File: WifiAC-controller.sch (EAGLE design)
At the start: 10 parts

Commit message: fixed schematic and generated layout
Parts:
- DRV_PINS, PWR_IN: device SparkFun-Connectors:M02PTH3 -> SparkFun-Connectors:M02LOCK_LONGPADS
- R2: device SparkFun-Resistors:RESISTOR1206 -> SparkFun-Resistors:RESISTORPTH-1/4W
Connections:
- net GPIO12: now also QBS_B.C; no longer QBS_C.B
- net GPIO13: now also QBS_C.C; no longer QBS_D.B
- net GPIO14: now also QBS_D.C; no longer QBS_B.B
- net GPIO16: now also QBS_A.C; no longer QBS_A.B
- net P59: now also QBS_C.B, QBS_D.B; no longer QBS_C.C, QBS_D.C
- net P7: now also QBS_A.B, QBS_B.B; no longer QBS_A.C, QBS_B.C

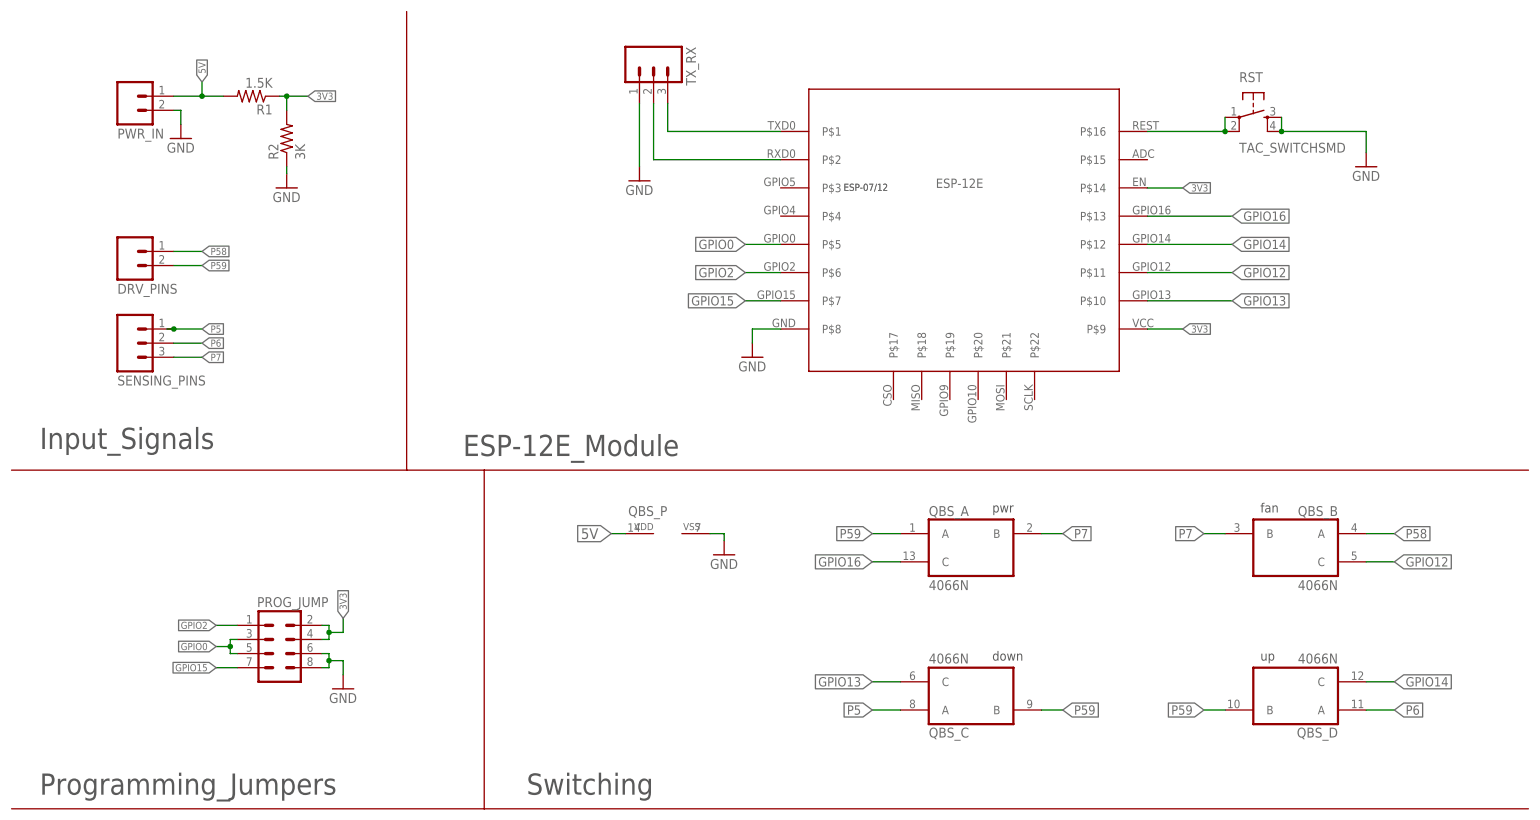
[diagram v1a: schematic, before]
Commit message: updated schematic to add input connections for the esp module
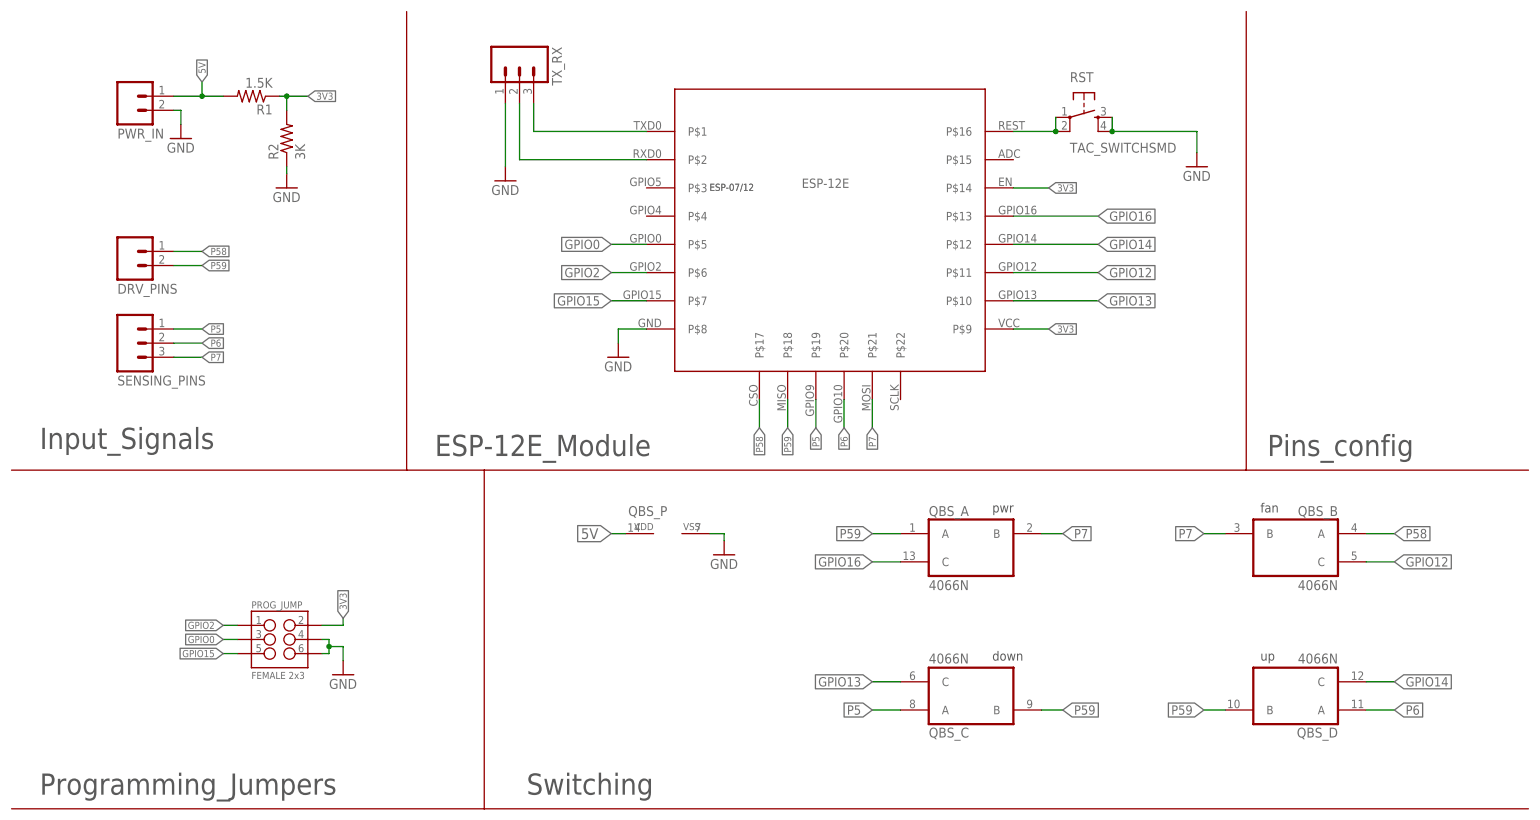
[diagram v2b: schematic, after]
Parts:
- PROG_JUMP: value (none) -> FEMALE 2x3; device SparkFun-Connectors:M04X2 -> SparkFun-Connectors:M03X2FEMALE
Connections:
- net 3V3: no longer PROG_JUMP.4
- net GND: now also PROG_JUMP.4; no longer PROG_JUMP.8
- net GPIO0: no longer PROG_JUMP.5
- net GPIO15: now also PROG_JUMP.5; no longer PROG_JUMP.7
- net P5: now also ESP-12E.P$19
- net P58: now also ESP-12E.P$17
- net P59: now also ESP-12E.P$18
- net P6: now also ESP-12E.P$20
- net P7: now also ESP-12E.P$21
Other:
- note added: "INPUT PINS"
- note added: "OUTPUT PINS"
- note added: "Pins_config"
- note added: "down -> GPIO13"
- note added: "fan -> GPIO12"
- note added: "p5 -> GPIO9"
- note added: "p58 -> GPIO11"
- note added: "p59 -> GPIO7"
- note added: "p6 -> GPIO10"
- note added: "p7 -> GPIO8"
- note added: "pwr -> GPIO16"
- note added: "up -> GPIO14"
- moved on the sheet: RST, TX_RX

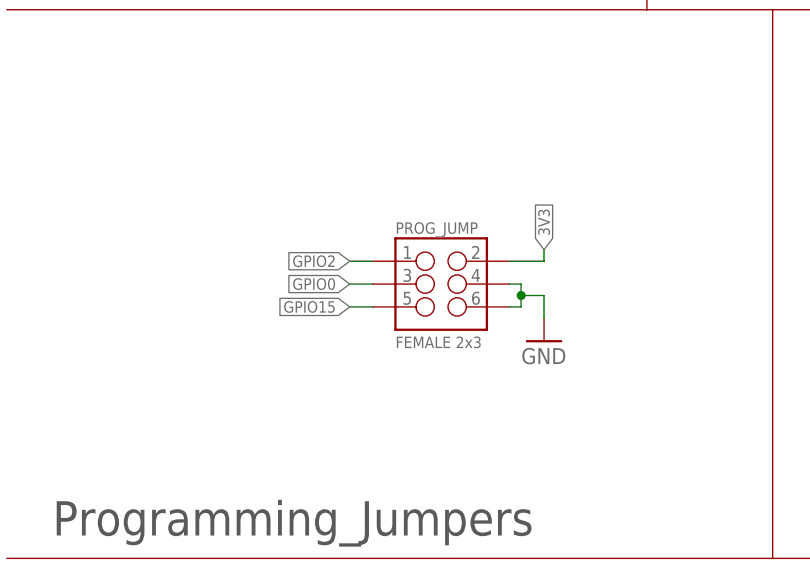
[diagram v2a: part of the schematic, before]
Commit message: updated layout
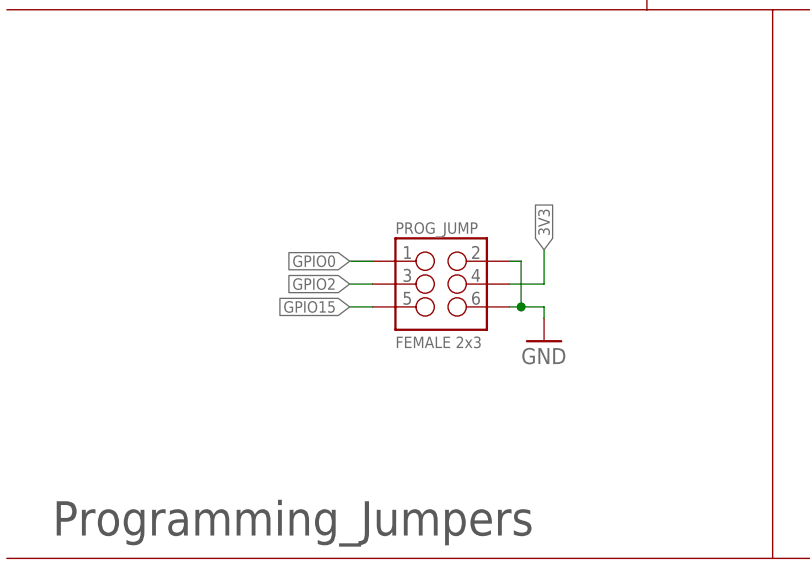
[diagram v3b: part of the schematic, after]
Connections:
- net 3V3: now also PROG_JUMP.4; no longer PROG_JUMP.2
- net GND: now also PROG_JUMP.2; no longer PROG_JUMP.4
- net GPIO0: now also PROG_JUMP.1; no longer PROG_JUMP.3
- net GPIO2: now also PROG_JUMP.3; no longer PROG_JUMP.1
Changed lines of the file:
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@@
 </segment>
 <segment>
-<pinref part="PROG_JUMP" gate="G$1" pin="2"/>
-<wire x1="55.88" y1="68.58" x2="59.69" y2="68.58" width="0.1524" layer="91"/>
-<wire x1="59.69" y1="68.58" x2="59.69" y2="69.85" width="0.1524" layer="91"/>
 <label x="59.69" y="69.85" size="1.27" layer="95" font="vector" rot="R90" xref="yes"/>
+<wire x1="59.69" y1="69.85" x2="59.69" y2="66.04" width="0.1524" layer="91"/>
+<pinref part="PROG_JUMP" gate="G$1" pin="4"/>
+<wire x1="59.69" y1="66.04" x2="55.88" y2="66.04" width="0.1524" layer="91"/>
 </segment>
 </net>
@@
 </segment>
 <segment>
-<wire x1="57.15" y1="64.77" x2="59.69" y2="64.77" width="0.1524" layer="91"/>
-<wire x1="59.69" y1="64.77" x2="59.69" y2="62.23" width="0.1524" layer="91"/>
+<wire x1="55.88" y1="63.5" x2="57.15" y2="63.5" width="0.1524" layer="91"/>
+<wire x1="57.15" y1="63.5" x2="59.69" y2="63.5" width="0.1524" layer="91"/>
+<wire x1="59.69" y1="63.5" x2="59.69" y2="62.23" width="0.1524" layer="91"/>
 <pinref part="GND6" gate="1" pin="GND"/>
-<pinref part="PROG_JUMP" gate="G$1" pin="4"/>
-<wire x1="55.88" y1="66.04" x2="57.15" y2="66.04" width="0.1524" layer="91"/>
-<wire x1="57.15" y1="66.04" x2="57.15" y2="64.77" width="0.1524" layer="91"/>
 <pinref part="PROG_JUMP" gate="G$1" pin="6"/>
-<wire x1="55.88" y1="63.5" x2="57.15" y2="63.5" width="0.1524" layer="91"/>
-<wire x1="57.15" y1="63.5" x2="57.15" y2="64.77" width="0.1524" layer="91"/>
-<junction x="57.15" y="64.77"/>
+<pinref part="PROG_JUMP" gate="G$1" pin="2"/>
+<wire x1="55.88" y1="68.58" x2="57.15" y2="68.58" width="0.1524" layer="91"/>
+<wire x1="57.15" y1="68.58" x2="57.15" y2="63.5" width="0.1524" layer="91"/>
+<junction x="57.15" y="63.5"/>
 </segment>
 <segment>
@@
 </segment>
 <segment>
+<pinref part="PROG_JUMP" gate="G$1" pin="1"/>
+<wire x1="40.64" y1="68.58" x2="38.1" y2="68.58" width="0.1524" layer="91"/>
+<label x="38.1" y="68.58" size="1.27" layer="95" rot="R180" xref="yes"/>
+</segment>
+</net>
+<net name="GPIO2" class="0">
+<segment>
+<pinref part="ESP-12E" gate="G$1" pin="P$6"/>
+<wire x1="114.3" y1="132.08" x2="107.95" y2="132.08" width="0.1524" layer="91"/>
+<label x="107.95" y="132.08" size="1.6764" layer="95" rot="R180" xref="yes"/>
+</segment>
+<segment>
 <pinref part="PROG_JUMP" gate="G$1" pin="3"/>
 <wire x1="40.64" y1="66.04" x2="38.1" y2="66.04" width="0.1524" layer="91"/>
@@
 </segment>
 </net>
-<net name="GPIO2" class="0">
-<segment>
-<pinref part="ESP-12E" gate="G$1" pin="P$6"/>
-<wire x1="114.3" y1="132.08" x2="107.95" y2="132.08" width="0.1524" layer="91"/>
-<label x="107.95" y="132.08" size="1.6764" layer="95" rot="R180" xref="yes"/>
-</segment>
-<segment>
-<pinref part="PROG_JUMP" gate="G$1" pin="1"/>
-<wire x1="40.64" y1="68.58" x2="38.1" y2="68.58" width="0.1524" layer="91"/>
-<label x="38.1" y="68.58" size="1.27" layer="95" rot="R180" xref="yes"/>
-</segment>
-</net>

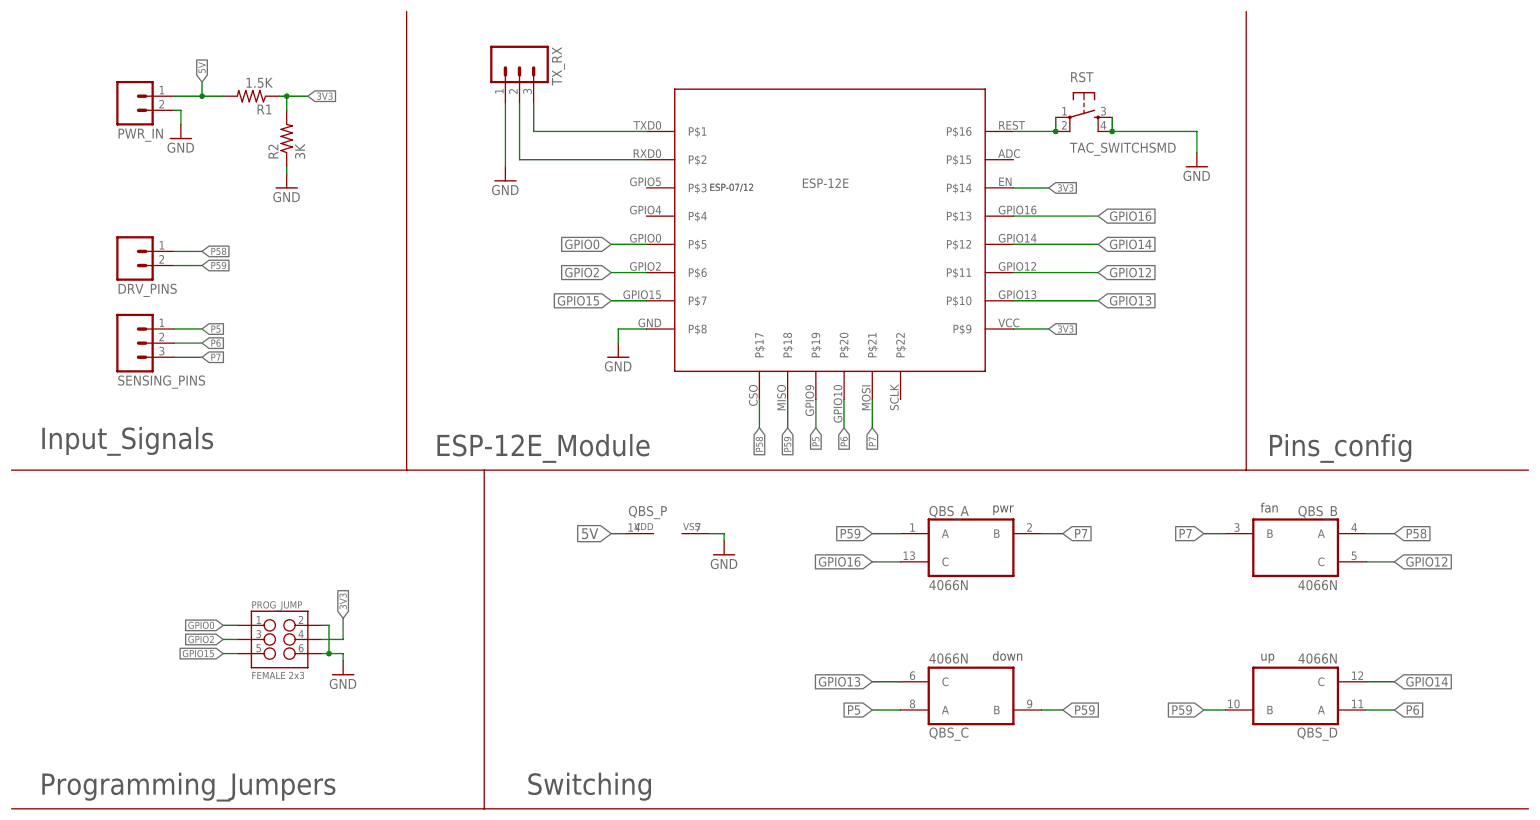
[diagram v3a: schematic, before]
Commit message: fixed GPIO connections and regenerated mill path with initial code added
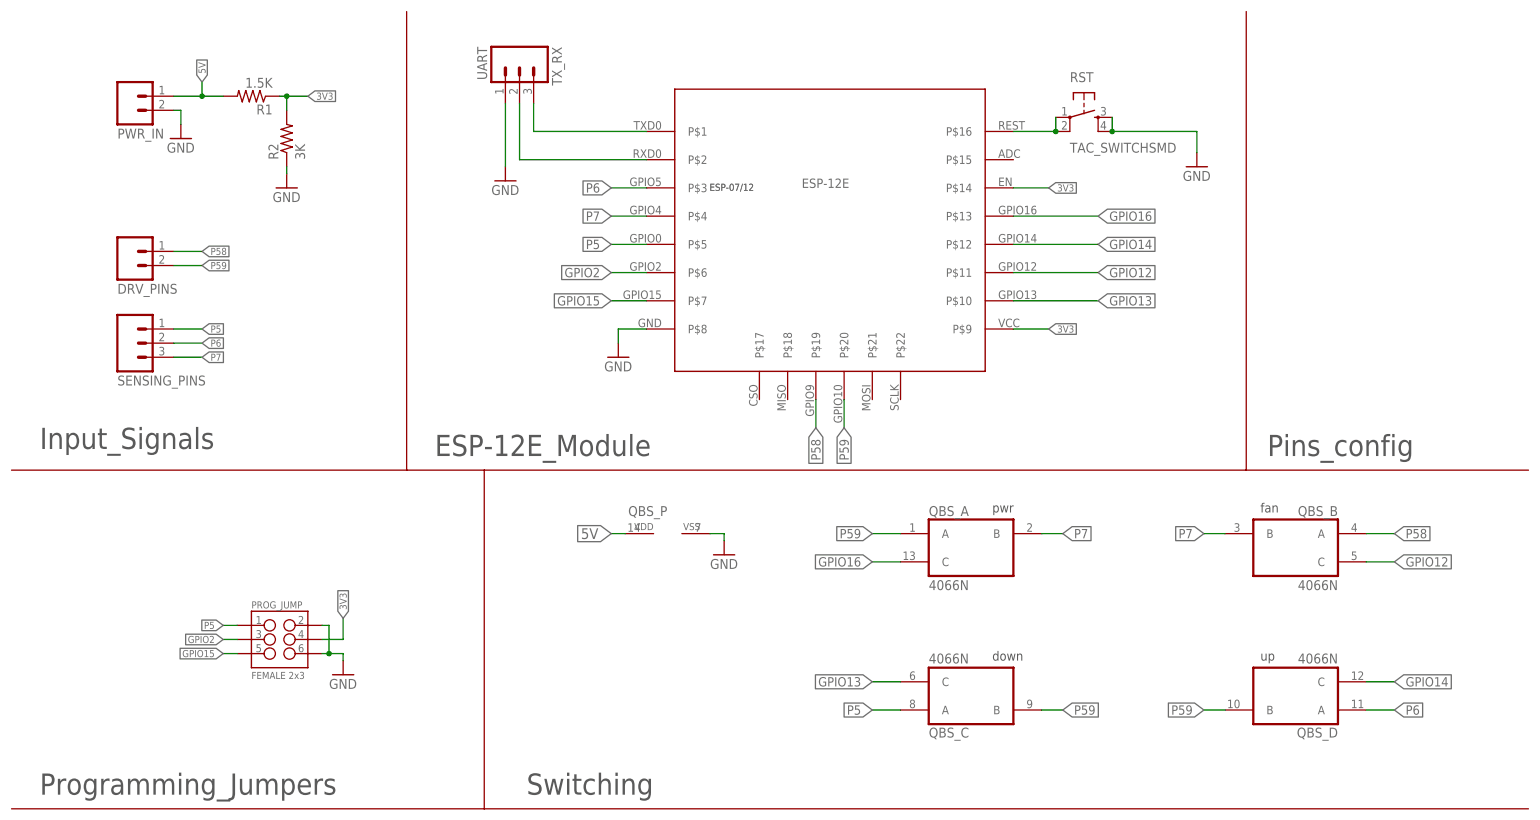
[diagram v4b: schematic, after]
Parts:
- TX_RX: value (none) -> UART
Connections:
- removed net GPIO0: ESP-12E.P$5, PROG_JUMP.1
- net P5: now also ESP-12E.P$5, PROG_JUMP.1; no longer ESP-12E.P$19
- net P58: now also ESP-12E.P$19; no longer ESP-12E.P$17
- net P59: now also ESP-12E.P$20; no longer ESP-12E.P$18
- net P6: now also ESP-12E.P$3; no longer ESP-12E.P$20
- net P7: now also ESP-12E.P$4; no longer ESP-12E.P$21
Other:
- note added: "p5 -> GPIO0"
- note added: "p58 -> GPIO9"
- note added: "p59 -> GPIO10"
- note added: "p6 -> GPIO5"
- note added: "p7 -> GPIO4"
- note removed: "p5 -> GPIO9"
- note removed: "p58 -> GPIO11"
- note removed: "p59 -> GPIO7"
- note removed: "p6 -> GPIO10"
- note removed: "p7 -> GPIO8"
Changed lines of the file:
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@@
 <setting verticaltext="up"/>
 </settings>
-<grid distance="0.05" unitdist="inch" unit="inch" style="lines" multiple="1" display="yes" altdistance="0.0025" altunitdist="inch" altunit="inch"/>
+<grid distance="0.1" unitdist="inch" unit="inch" style="lines" multiple="1" display="no" altdistance="0.01" altunitdist="inch" altunit="inch"/>
 <layers>
 <layer number="1" name="Top" color="4" fill="1" visible="no" active="no"/>
@@
 <part name="RST" library="SparkFun-Retired" deviceset="TAC_SWITCH" device="SMD" value="TAC_SWITCHSMD"/>
 <part name="GND4" library="SparkFun-Aesthetics" deviceset="GND" device=""/>
-<part name="TX_RX" library="SparkFun-Connectors" deviceset="M03" device="LONGPADS"/>
+<part name="TX_RX" library="SparkFun-Connectors" deviceset="M03" device="LONGPADS" value="UART"/>
 <part name="GND5" library="SparkFun-Aesthetics" deviceset="GND" device=""/>
 <part name="PROG_JUMP" library="SparkFun-Connectors" deviceset="M03X2" device="FEMALE" value="FEMALE 2x3"/>
@@
 <text x="5.08" y="25.4" size="2.1844" layer="114" font="vector">The PROG_JUMP is a jumper used to change the mode of the chip in case a reprogramming is needed.</text>
 <text x="5.08" y="20.32" size="2.1844" layer="114" font="vector">The ESP packge is imported from the lib ESP-12.lbr</text>
-<text x="228.6" y="162.56" size="2.54" layer="114">p58 -&gt; GPIO11</text>
-<text x="228.6" y="157.48" size="2.54" layer="114">p59 -&gt; GPIO7</text>
-<text x="228.6" y="152.4" size="2.54" layer="114">p5 -&gt; GPIO9</text>
-<text x="228.6" y="147.32" size="2.54" layer="114">p6 -&gt; GPIO10</text>
-<text x="228.6" y="142.24" size="2.54" layer="114">p7 -&gt; GPIO8</text>
+<text x="228.6" y="162.56" size="2.54" layer="114">p58 -&gt; GPIO9</text>
+<text x="228.6" y="157.48" size="2.54" layer="114">p59 -&gt; GPIO10</text>
+<text x="228.6" y="152.4" size="2.54" layer="114">p5 -&gt; GPIO0</text>
+<text x="228.6" y="147.32" size="2.54" layer="114">p6 -&gt; GPIO5</text>
+<text x="228.6" y="142.24" size="2.54" layer="114">p7 -&gt; GPIO4</text>
 <wire x1="222.25" y1="179.07" x2="222.25" y2="96.52" width="0.1524" layer="94"/>
 <text x="228.6" y="128.27" size="2.54" layer="114">pwr -&gt; GPIO16</text>
@@
 </segment>
 <segment>
-<pinref part="ESP-12E" gate="G$1" pin="P$17"/>
-<wire x1="134.62" y1="109.22" x2="134.62" y2="104.14" width="0.1524" layer="91"/>
-<label x="134.62" y="104.14" size="1.27" layer="95" rot="R270" xref="yes"/>
+<pinref part="ESP-12E" gate="G$1" pin="P$19"/>
+<wire x1="144.78" y1="109.22" x2="144.78" y2="104.14" width="0.1524" layer="91"/>
+<label x="144.78" y="104.14" size="1.6764" layer="95" rot="R270" xref="yes"/>
 </segment>
 </net>
@@
 </segment>
 <segment>
-<pinref part="ESP-12E" gate="G$1" pin="P$18"/>
-<wire x1="139.7" y1="109.22" x2="139.7" y2="104.14" width="0.1524" layer="91"/>
-<label x="139.7" y="104.14" size="1.27" layer="95" rot="R270" xref="yes"/>
+<pinref part="ESP-12E" gate="G$1" pin="P$20"/>
+<wire x1="149.86" y1="109.22" x2="149.86" y2="104.14" width="0.1524" layer="91"/>
+<label x="149.86" y="104.14" size="1.6764" layer="95" rot="R270" xref="yes"/>
 </segment>
 </net>
@@
 </segment>
 <segment>
-<pinref part="ESP-12E" gate="G$1" pin="P$19"/>
-<wire x1="144.78" y1="109.22" x2="144.78" y2="104.14" width="0.1524" layer="91"/>
-<label x="144.78" y="104.14" size="1.27" layer="95" rot="R270" xref="yes"/>
+<pinref part="PROG_JUMP" gate="G$1" pin="1"/>
+<wire x1="40.64" y1="68.58" x2="38.1" y2="68.58" width="0.1524" layer="91"/>
+<label x="38.1" y="68.58" size="1.27" layer="95" rot="R180" xref="yes"/>
+</segment>
+<segment>
+<pinref part="ESP-12E" gate="G$1" pin="P$5"/>
+<wire x1="114.3" y1="137.16" x2="107.95" y2="137.16" width="0.1524" layer="91"/>
+<label x="107.95" y="137.16" size="1.6764" layer="95" rot="R180" xref="yes"/>
 </segment>
 </net>
@@
 </segment>
 <segment>
-<pinref part="ESP-12E" gate="G$1" pin="P$20"/>
-<wire x1="149.86" y1="109.22" x2="149.86" y2="104.14" width="0.1524" layer="91"/>
-<label x="149.86" y="104.14" size="1.27" layer="95" rot="R270" xref="yes"/>
+<pinref part="ESP-12E" gate="G$1" pin="P$3"/>
+<wire x1="114.3" y1="147.32" x2="107.95" y2="147.32" width="0.1524" layer="91"/>
+<label x="107.95" y="147.32" size="1.6764" layer="95" rot="R180" xref="yes"/>
 </segment>
 </net>
@@
 </segment>
 <segment>
-<pinref part="ESP-12E" gate="G$1" pin="P$21"/>
-<wire x1="154.94" y1="109.22" x2="154.94" y2="104.14" width="0.1524" layer="91"/>
-<label x="154.94" y="104.14" size="1.27" layer="95" rot="R270" xref="yes"/>
+<pinref part="ESP-12E" gate="G$1" pin="P$4"/>
+<wire x1="114.3" y1="142.24" x2="107.95" y2="142.24" width="0.1524" layer="91"/>
+<label x="107.95" y="142.24" size="1.6764" layer="95" rot="R180" xref="yes"/>
 </segment>
 </net>
@@
 </segment>
 </net>
-<net name="GPIO0" class="0">
-<segment>
-<pinref part="ESP-12E" gate="G$1" pin="P$5"/>
-<wire x1="114.3" y1="137.16" x2="107.95" y2="137.16" width="0.1524" layer="91"/>
-<label x="107.95" y="137.16" size="1.6764" layer="95" rot="R180" xref="yes"/>
-</segment>
-<segment>
-<pinref part="PROG_JUMP" gate="G$1" pin="1"/>
-<wire x1="40.64" y1="68.58" x2="38.1" y2="68.58" width="0.1524" layer="91"/>
-<label x="38.1" y="68.58" size="1.27" layer="95" rot="R180" xref="yes"/>
-</segment>
-</net>
